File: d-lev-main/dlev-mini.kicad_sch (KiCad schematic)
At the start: 43 parts, among them J1 S6B-PH-SM4-TB, J2 S8B-PH-SM4-TB, J3 S8B-PH-SM4-TB, J4 S12B-PH-SM4-TB, U3 AMS1117-3.3

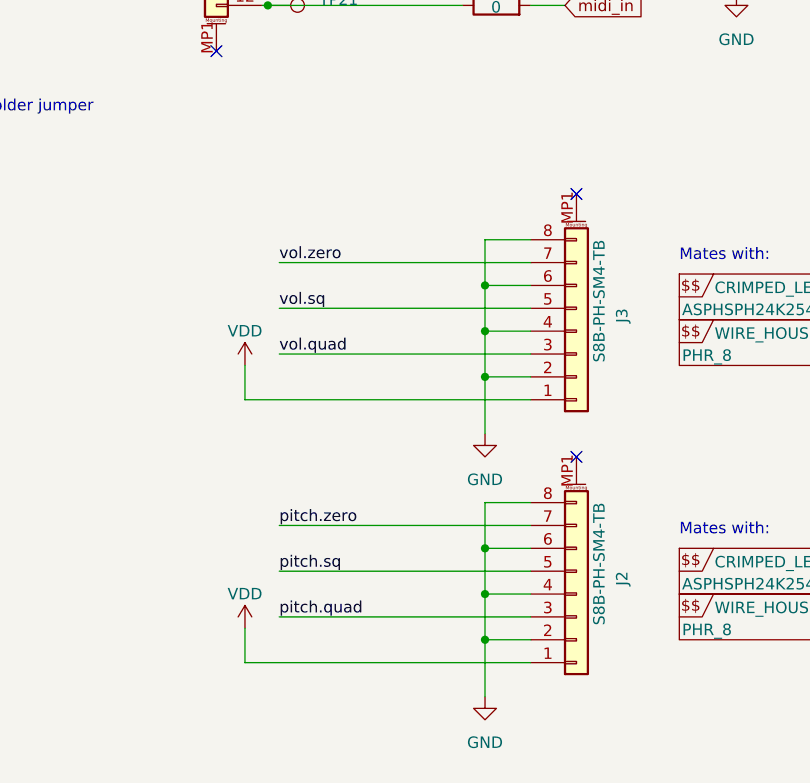
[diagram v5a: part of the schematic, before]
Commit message: d-lev-main: de-round tracks
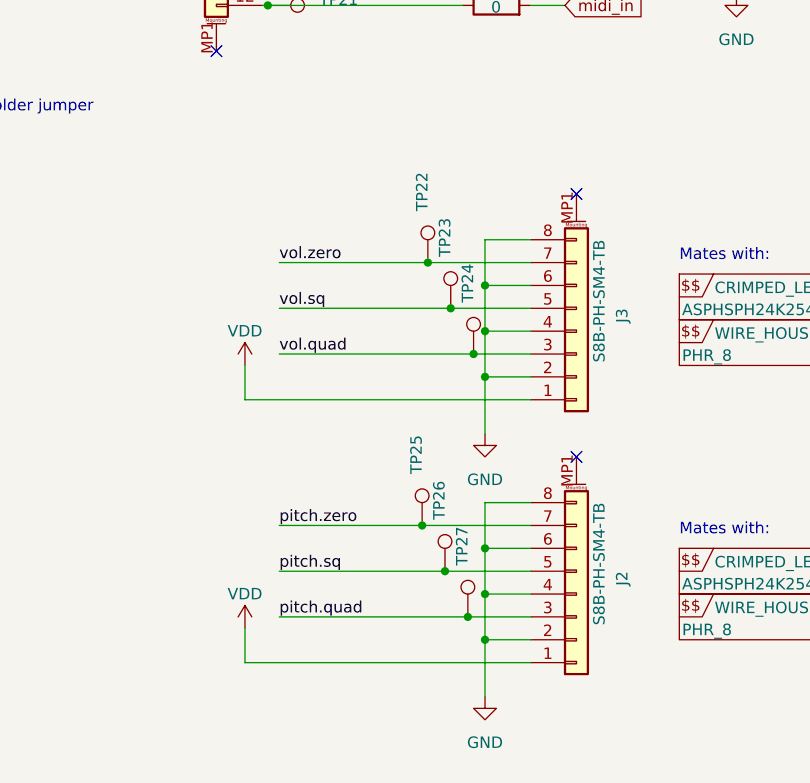
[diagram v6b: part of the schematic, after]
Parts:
- added TP22, TP23, TP24, TP25, TP26, TP27: TestPoint, TestPoint:TestPoint_Pad_D1.0mm, symbol Connector:TestPoint
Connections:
- net pitch.quad: now also TP27.1
- net pitch.sq: now also TP26.1
- net pitch.zero: now also TP25.1
- net vol.quad: now also TP24.1
- net vol.sq: now also TP23.1
- net vol.zero: now also TP22.1
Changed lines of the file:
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@@
   (junction (at 203.835 77.47) (diameter 0) (color 0 0 0 0)
   )
+  (junction (at 221.615 108.585) (diameter 0) (color 0 0 0 0)
+  )
   (junction (at 59.055 45.72) (diameter 0) (color 0 0 0 0)
   )
@@
   (junction (at 203.835 62.23) (diameter 0) (color 0 0 0 0)
   )
+  (junction (at 223.52 142.875) (diameter 0) (color 0 0 0 0)
+  )
   (junction (at 37.465 45.72) (diameter 0) (color 0 0 0 0)
   )
@@
   (junction (at 46.355 58.42) (diameter 0) (color 0 0 0 0)
   )
+  (junction (at 226.06 147.955) (diameter 0) (color 0 0 0 0)
+  )
   (junction (at 227.965 140.335) (diameter 0) (color 0 0 0 0)
   )
@@
   (junction (at 227.965 150.495) (diameter 0) (color 0 0 0 0)
   )
+  (junction (at 226.695 118.745) (diameter 0) (color 0 0 0 0)
+  )
   (junction (at 227.965 111.125) (diameter 0) (color 0 0 0 0)
   )
@@
   (junction (at 33.655 58.42) (diameter 0) (color 0 0 0 0)
   )
+  (junction (at 224.155 113.665) (diameter 0) (color 0 0 0 0)
+  )
   (junction (at 227.965 116.205) (diameter 0) (color 0 0 0 0)
   )
@@
   )
   (junction (at 203.835 64.77) (diameter 0) (color 0 0 0 0)
+  )
+  (junction (at 220.98 137.795) (diameter 0) (color 0 0 0 0)
   )
   (junction (at 227.965 145.415) (diameter 0) (color 0 0 0 0)
@@
     (stroke (width 0) (type default))
   )
+  (wire (pts (xy 226.695 118.745) (xy 233.045 118.745))
+    (stroke (width 0) (type default))
+  )
   (wire (pts (xy 46.355 58.42) (xy 46.355 60.96))
     (stroke (width 0) (type default))
@@
     (stroke (width 0) (type default))
   )
-  (wire (pts (xy 205.105 147.955) (xy 233.045 147.955))
+  (wire (pts (xy 205.105 147.955) (xy 226.06 147.955))
     (stroke (width 0) (type default))
   )
@@
     (stroke (width 0) (type default))
   )
+  (wire (pts (xy 226.06 147.955) (xy 233.045 147.955))
+    (stroke (width 0) (type default))
+  )
   (polyline (pts (xy 131.826 -37.846) (xy 133.096 -39.116))
     (stroke (width 0) (type default))
@@
     (stroke (width 0) (type default))
   )
+  (wire (pts (xy 220.98 137.795) (xy 233.045 137.795))
+    (stroke (width 0) (type default))
+  )
   (wire (pts (xy 119.38 24.13) (xy 119.38 26.67))
     (stroke (width 0) (type default))
@@
     (stroke (width 0) (type default))
   )
-  (wire (pts (xy 205.105 142.875) (xy 233.045 142.875))
+  (wire (pts (xy 205.105 142.875) (xy 223.52 142.875))
     (stroke (width 0) (type default))
   )
@@
     (stroke (width 0) (type default))
   )
+  (wire (pts (xy 223.52 142.875) (xy 233.045 142.875))
+    (stroke (width 0) (type default))
+  )
   (wire (pts (xy 33.655 45.72) (xy 33.655 41.91))
     (stroke (width 0) (type default))
@@
     (stroke (width 0) (type default))
   )
-  (wire (pts (xy 205.105 113.665) (xy 233.045 113.665))
+  (wire (pts (xy 205.105 113.665) (xy 224.155 113.665))
     (stroke (width 0) (type default))
   )
@@
     (stroke (width 0) (type default))
   )
-  (wire (pts (xy 205.105 118.745) (xy 233.045 118.745))
+  (wire (pts (xy 205.105 118.745) (xy 226.695 118.745))
     (stroke (width 0) (type default))
   )
@@
     (stroke (width 0) (type default))
   )
+  (wire (pts (xy 224.155 113.665) (xy 233.045 113.665))
+    (stroke (width 0) (type default))
+  )
   (polyline (pts (xy 17.526 -35.306) (xy 16.256 -34.036))
     (stroke (width 0) (type default))
@@
     (stroke (width 0) (type default))
   )
-  (wire (pts (xy 205.105 137.795) (xy 233.045 137.795))
+  (wire (pts (xy 205.105 137.795) (xy 220.98 137.795))
     (stroke (width 0) (type default))
   )
@@
     (stroke (width 0) (type default))
   )
-  (wire (pts (xy 205.105 108.585) (xy 233.045 108.585))
+  (wire (pts (xy 205.105 108.585) (xy 221.615 108.585))
     (stroke (width 0) (type default))
   )
@@
   )
   (polyline (pts (xy 231.2162 -34.29) (xy 229.9462 -33.02))
+    (stroke (width 0) (type default))
+  )
+  (wire (pts (xy 221.615 108.585) (xy 233.045 108.585))
     (stroke (width 0) (type default))
   )
@@
     )
   )
+  (symbol (lib_id "Connector:TestPoint") (at 223.52 142.875 0) (unit 1)
+    (in_bom yes) (on_board yes) (dnp no)
+    (property "Reference" "TP26" (at 222.885 137.16 90)
+      (effects (font (size 1.27 1.27)) (justify left))
+    )
+    (property "Value" "TestPoint" (at 225.425 137.16 90)
+      (effects (font (size 1.27 1.27)) (justify left) hide)
+    )
+    (property "Footprint" "TestPoint:TestPoint_Pad_D1.0mm" (at 228.6 142.875 0)
+      (effects (font (size 1.27 1.27)) hide)
+    )
+    (property "Datasheet" "~" (at 228.6 142.875 0)
+      (effects (font (size 1.27 1.27)) hide)
+    )
+    (pin "1")
+    (instances
+      (project "dlev-mini"
+        (path "/eb5e8bfd-9871-4528-bf57-58851bf63907"
+          (reference "TP26") (unit 1)
+        )
+      )
+    )
+  )
+  (symbol (lib_id "Connector:TestPoint") (at 224.155 113.665 0) (unit 1)
+    (in_bom yes) (on_board yes) (dnp no)
+    (property "Reference" "TP23" (at 223.52 107.95 90)
+      (effects (font (size 1.27 1.27)) (justify left))
+    )
+    (property "Value" "TestPoint" (at 226.06 107.95 90)
+      (effects (font (size 1.27 1.27)) (justify left) hide)
+    )
+    (property "Footprint" "TestPoint:TestPoint_Pad_D1.0mm" (at 229.235 113.665 0)
+      (effects (font (size 1.27 1.27)) hide)
+    )
+    (property "Datasheet" "~" (at 229.235 113.665 0)
+      (effects (font (size 1.27 1.27)) hide)
+    )
+    (pin "1")
+    (instances
+      (project "dlev-mini"
+        (path "/eb5e8bfd-9871-4528-bf57-58851bf63907"
+          (reference "TP23") (unit 1)
+        )
+      )
+    )
+  )
+  (symbol (lib_id "Connector:TestPoint") (at 220.98 137.795 0) (unit 1)
+    (in_bom yes) (on_board yes) (dnp no)
+    (property "Reference" "TP25" (at 220.345 132.08 90)
+      (effects (font (size 1.27 1.27)) (justify left))
+    )
+    (property "Value" "TestPoint" (at 222.885 132.08 90)
+      (effects (font (size 1.27 1.27)) (justify left) hide)
+    )
+    (property "Footprint" "TestPoint:TestPoint_Pad_D1.0mm" (at 226.06 137.795 0)
+      (effects (font (size 1.27 1.27)) hide)
+    )
+    (property "Datasheet" "~" (at 226.06 137.795 0)
+      (effects (font (size 1.27 1.27)) hide)
+    )
+    (pin "1")
+    (instances
+      (project "dlev-mini"
+        (path "/eb5e8bfd-9871-4528-bf57-58851bf63907"
+          (reference "TP25") (unit 1)
+        )
+      )
+    )
+  )
   (symbol (lib_id "assorted:Conn_01x08_MountingPin") (at 238.125 145.415 0) (mirror x) (unit 1)
     (in_bom yes) (on_board yes) (dnp no)
@@
     )
   )
+  (symbol (lib_id "Connector:TestPoint") (at 221.615 108.585 0) (unit 1)
+    (in_bom yes) (on_board yes) (dnp no)
+    (property "Reference" "TP22" (at 220.98 102.87 90)
+      (effects (font (size 1.27 1.27)) (justify left))
+    )
+    (property "Value" "TestPoint" (at 223.52 102.87 90)
+      (effects (font (size 1.27 1.27)) (justify left) hide)
+    )
+    (property "Footprint" "TestPoint:TestPoint_Pad_D1.0mm" (at 226.695 108.585 0)
+      (effects (font (size 1.27 1.27)) hide)
+    )
+    (property "Datasheet" "~" (at 226.695 108.585 0)
+      (effects (font (size 1.27 1.27)) hide)
+    )
+    (pin "1")
+    (instances
+      (project "dlev-mini"
+        (path "/eb5e8bfd-9871-4528-bf57-58851bf63907"
+          (reference "TP22") (unit 1)
+        )
+      )
+    )
+  )
   (symbol (lib_id "power:VDD") (at 201.295 149.225 0) (unit 1)
     (in_bom yes) (on_board yes) (dnp no) (fields_autoplaced)
@@
     )
   )
+  (symbol (lib_id "Connector:TestPoint") (at 226.695 118.745 0) (unit 1)
+    (in_bom yes) (on_board yes) (dnp no)
+    (property "Reference" "TP24" (at 226.06 113.03 90)
+      (effects (font (size 1.27 1.27)) (justify left))
+    )
+    (property "Value" "TestPoint" (at 228.6 113.03 90)
+      (effects (font (size 1.27 1.27)) (justify left) hide)
+    )
+    (property "Footprint" "TestPoint:TestPoint_Pad_D1.0mm" (at 231.775 118.745 0)
+      (effects (font (size 1.27 1.27)) hide)
+    )
+    (property "Datasheet" "~" (at 231.775 118.745 0)
+      (effects (font (size 1.27 1.27)) hide)
+    )
+    (pin "1")
+    (instances
+      (project "dlev-mini"
+        (path "/eb5e8bfd-9871-4528-bf57-58851bf63907"
+          (reference "TP24") (unit 1)
+        )
+      )
+    )
+  )
   (symbol (lib_id "Mechanical:MountingHole_Pad") (at 252.095 16.51 0) (mirror y) (unit 1)
     (in_bom yes) (on_board yes) (dnp no) (fields_autoplaced)
@@
         )
       )
+    )
+  )
+  (symbol (lib_id "Connector:TestPoint") (at 226.06 147.955 0) (unit 1)
+    (in_bom yes) (on_board yes) (dnp no)
+    (property "Reference" "TP27" (at 225.425 142.24 90)
+      (effects (font (size 1.27 1.27)) (justify left))
+    )
+    (property "Value" "TestPoint" (at 227.965 142.24 90)
+      (effects (font (size 1.27 1.27)) (justify left) hide)
+    )
+    (property "Footprint" "TestPoint:TestPoint_Pad_D1.0mm" (at 231.14 147.955 0)
+      (effects (font (size 1.27 1.27)) hide)
+    )
+    (property "Datasheet" "~" (at 231.14 147.955 0)
+      (effects (font (size 1.27 1.27)) hide)
+    )
+    (pin "1")
+    (instances
+      (project "dlev-mini"
+        (path "/eb5e8bfd-9871-4528-bf57-58851bf63907"
+          (reference "TP27") (unit 1)
+        )
+      )
